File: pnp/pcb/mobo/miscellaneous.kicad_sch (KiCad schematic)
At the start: 10 parts

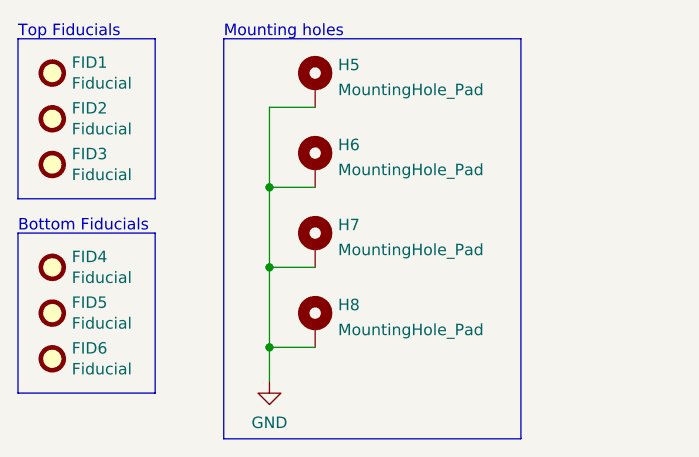
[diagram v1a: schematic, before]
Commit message: Redesign finished
Completed Board redesign and adding more EMC improvements.
Changed all the part numbers to have a Mouser orderable design (except the JST connectors)
All outputs generated
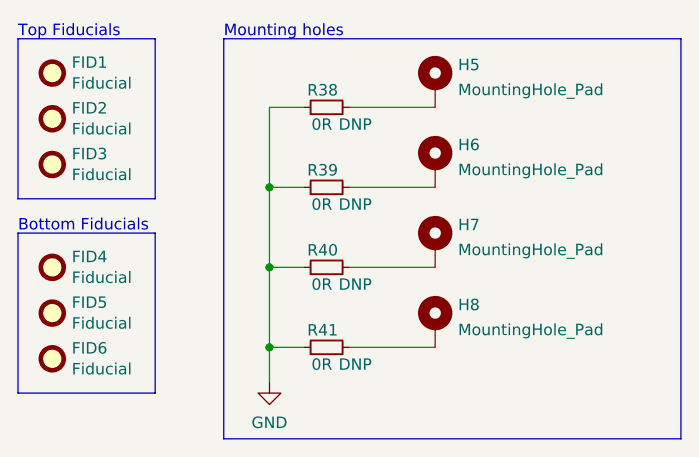
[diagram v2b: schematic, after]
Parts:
- added R38, R39, R40, R41: 0R, Resistor_SMD:R_0805_2012Metric, symbol Device:R_Small
- FID1, FID2, FID3, FID4, FID5, FID6, H5, H6, H7, H8: Mouser (none) -> -
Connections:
- net GND: now also R38.1, R39.1, R40.1, R41.1; no longer H5.1, H6.1, H7.1, H8.1
- new net: H5.1, R38.2
- new net: H6.1, R39.2
- new net: H8.1, R41.2
- new net: H7.1, R40.2
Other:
- company: Opulo -> Opulo.io
- moved on the sheet: H5, H6, H7, H8
